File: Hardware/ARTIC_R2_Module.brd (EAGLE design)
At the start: 21.6 x 33 mm, 94 parts, among them J1 U.FL, K1 TLP3475R, Q2 5.8A/30V/35mΩ, U1 ADM4210-1, U2 1.8V/100mA, U3 ARTIC_R2, U4 RFPA0133, U5 AS179-92LF, U6 3.0V, X1 CRYSTAL-TCXO-26MHZ

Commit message: Work in progress
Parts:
- added J10, J11, J12, J13, J14, J15, J16, J17, J18, J19, J2, J20, J21, J22, J23, J24, J3, J4, J5, J6, J7, J8, J9: (no value), SparkFun-Connectors:1X01_NO_SILK
- added J25: U.FL, SparkFun-Connectors:U.FL
- added U$2: (no value), output:10
- J1: value U.FL -> (none); device SparkFun-Connectors:U.FL -> SparkFun-Connectors:1X01_NO_SILK
- moved J1 18.9 mm to (0.00, 30.5), turned to 0 degrees
- moved FD3 6.71 mm to (1.27, 1.27)
- moved FD4 6.71 mm to (1.27, 1.27)
- moved FD1 2.54 mm to (19.1, 31.8)
- moved FD2 2.54 mm to (19.1, 31.8)
- moved C3 1.97 mm to (6.35, 3.56)
- moved U2 1.97 mm to (4.25, 3.75)
- moved C45 1.89 mm to (8.38, 4.06)
- moved C2 1.80 mm to (10.0, 2.79)
- moved C23 1.69 mm to (11.8, 2.79)
- moved C49 1.69 mm to (9.53, 4.32)
- moved R11 1.69 mm to (10.5, 4.32)
- moved R12 1.69 mm to (12.8, 2.79)
- moved R2 1.69 mm to (12.3, 4.83)
- moved U1 1.69 mm to (16.1, 3.43)
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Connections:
- net ANTENNA: now also J23.1, J25.FEED; no longer J1.FEED
- net FLSH_CEN: now also J20.1
- net FLSH_SCLK: now also J17.1
- net FLSH_SI: now also J18.1
- net FLSH_SO: now also J19.1
- net GND: now also J16.1, J22.1, J24.1, J25.1, J25.2; no longer J1.1, J1.2
- net PWR_EN: now also J13.1
- net VDD: now also J21.1
- net VIN: now also J14.1, J15.1
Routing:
- net FLSH_CEN: track 0.00 -> 12.5 mm, vias 0 -> 1
- net FLSH_SO: track 0.00 -> 11.5 mm, vias 0 -> 1
- net FLSH_SI: track 0.00 -> 9.16 mm, vias 0 -> 1
- net FLSH_SCLK: track 0.00 -> 8.33 mm, vias 0 -> 1
- net VDD: track 74.1 -> 81.6 mm
- net PWR_EN: track 2.08 -> 8.60 mm
- net VIN: track 7.30 -> 12.2 mm
- net N$14: track 2.87 -> 6.70 mm
- net ANTENNA: track 1.54 -> 5.13 mm
- net 1.8V: track 64.0 -> 65.8 mm, vias 7 -> 8
- net N$2: track 4.50 -> 5.38 mm
- net N$3: track 7.92 -> 8.57 mm
- net GND: track 83.3 -> 83.4 mm, vias 103 -> 105
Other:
- board size 21.6 x 33 mm -> 20.3 x 33 mm
- board text added: "JLCPCB JLC7628 4-Layer 0.8mm Impedance Control 4-Layer Board 0.8mm Thickness 1oz Copper (Outer layers) ENIG Finish Castellated Holes When running the panelizer, add a horizontal gap of 0.5" to allow the castellated holes to be routed out"
- board text removed: "JLCPCB JLC7628 4-Layer 0.8mm Impedance Control 4-Layer Board 0.8mm Thickness 1oz Copper (Outer layers) ENIG Finish"

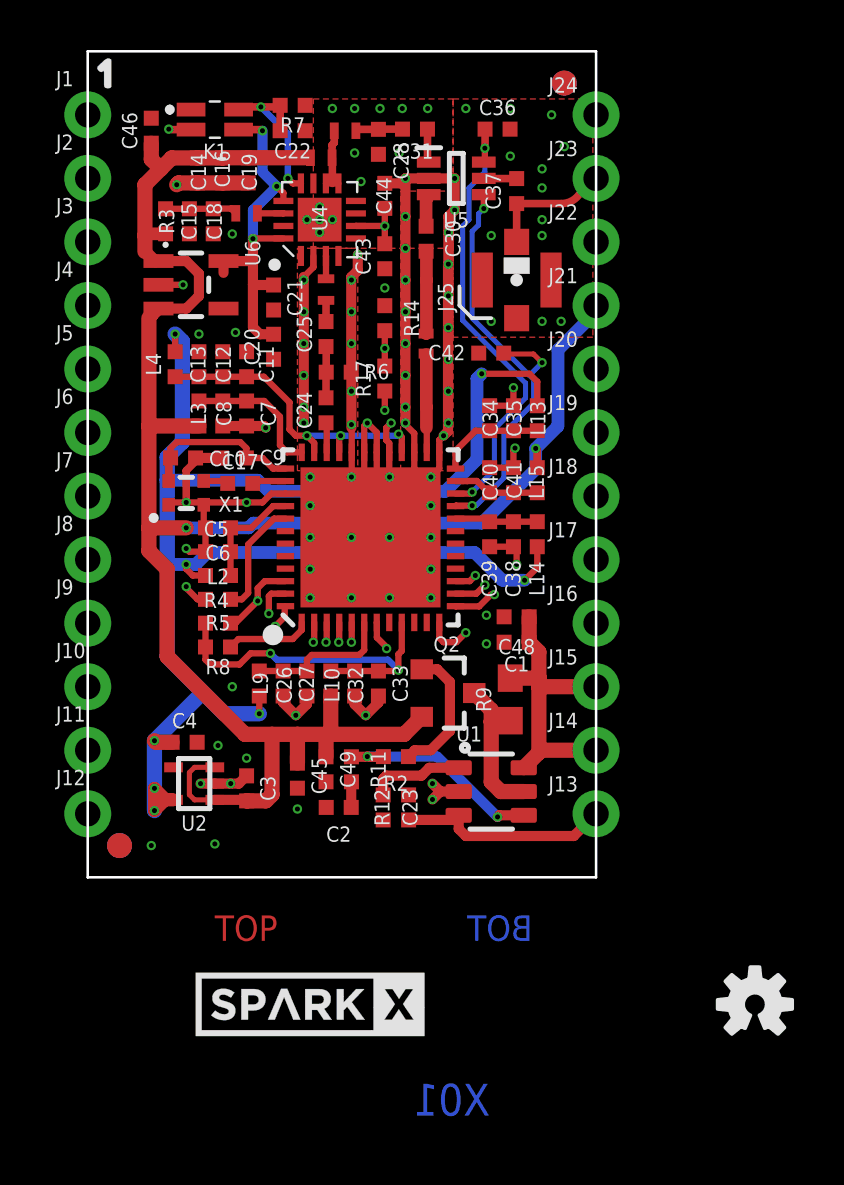
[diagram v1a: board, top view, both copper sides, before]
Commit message: Adding panel files. Updating README.
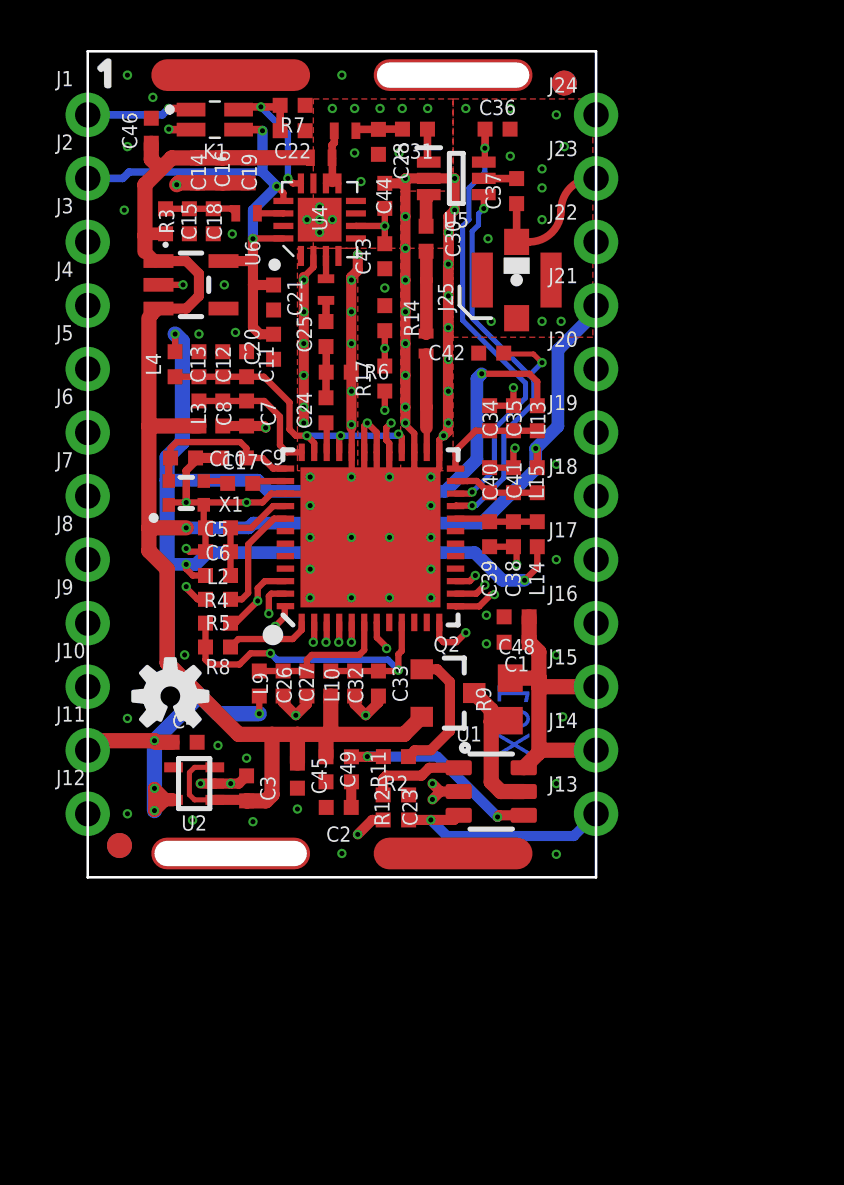
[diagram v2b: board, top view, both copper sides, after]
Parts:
- removed LOGO3: OSHW-LOGOS, SparkFun-Aesthetics:OSHW-LOGO-S
- removed SPARKX1, SPARKX2: SPARKX-LOGO4, SparkX:SPARKX-MEDIUM
- added SCREEN: ARTIC_R2_CASTELLATED_CAN, New_Parts_Screening_Cans:ARTIC_R2_CASTELLATED
- J1, J10, J11, J12, J13, J14, J15, J16, J17, J18, J19, J2, J20, J21, J22, J23, J24, J3, J4, J5, J6, J7, J8, J9: device SparkFun-Connectors:1X01_NO_SILK -> New_Parts_Connectors:1X01_CASTELLATED
- R9: value 0.012R -> 0.1R; device New_Parts:0603 -> New_Parts_Resistors:0603
- U1: device New_Parts:TSOT6 -> New_Parts_IC-Power:TSOT6
- moved LOGO2 26.4 mm to (3.30, 7.24)
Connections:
- net 1.8V: now also J11.1
- net BOOT: now also J3.1
- net CIPO: now also J10.1
- net COPI: now also J9.1
- net CS: now also J7.1
- net G8: now also J1.1
- net GND: now also J12.1, SCREEN.P$1, SCREEN.P$2, SCREEN.P$3, SCREEN.P$4
- net INT1: now also J4.1
- net INT2: now also J5.1
- net RESETB: now also J6.1
- net SCLK: now also J8.1
- net VREF1: now also J2.1
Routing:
- net BOOT: track 3.19 -> 22.2 mm
- net INT1: track 1.40 -> 19.0 mm
- net INT2: track 0.98 -> 16.9 mm
- net CS: track 0.81 -> 16.0 mm
- net RESETB: track 3.43 -> 17.4 mm
- net SCLK: track 0.80 -> 14.6 mm
- net COPI: track 0.80 -> 13.6 mm
- net CIPO: track 0.80 -> 13.6 mm
- net VREF1: track 15.6 -> 22.2 mm
- net PA_PD: track 16.4 -> 12.1 mm
- net G8: track 0.00 -> 4.25 mm, vias 0 -> 1
- net 1.8V: track 65.8 -> 68.6 mm
- net GND: track 83.4 -> 84.7 mm, vias 105 -> 120
- net PWR_EN: track 8.60 -> 9.32 mm, vias 0 -> 1
- net ANTENNA: track 5.13 -> 5.76 mm
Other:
- board text added: "Dimensions in Inches"
- board text added: "JLCPCB JLC7628 4-Layer 0.8mm Impedance Control 4-Layer Board 0.8mm Thickness 1oz Copper (Outer layers) ENIG Finish Castellated Holes When running the panelizer, add a vertical gap of 0.2" to allow the castellated holes to be routed out"
- board text removed: "15"
- board text removed: "2"
- board text removed: "BOT"
- board text removed: "JLCPCB JLC7628 4-Layer 0.8mm Impedance Control 4-Layer Board 0.8mm Thickness 1oz Copper (Outer layers) ENIG Finish Castellated Holes When running the panelizer, add a horizontal gap of 0.5" to allow the castellated holes to be routed out"
- board text removed: "TOP"

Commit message: Adding better castellated pads. Correcting cutouts for screen tabs.
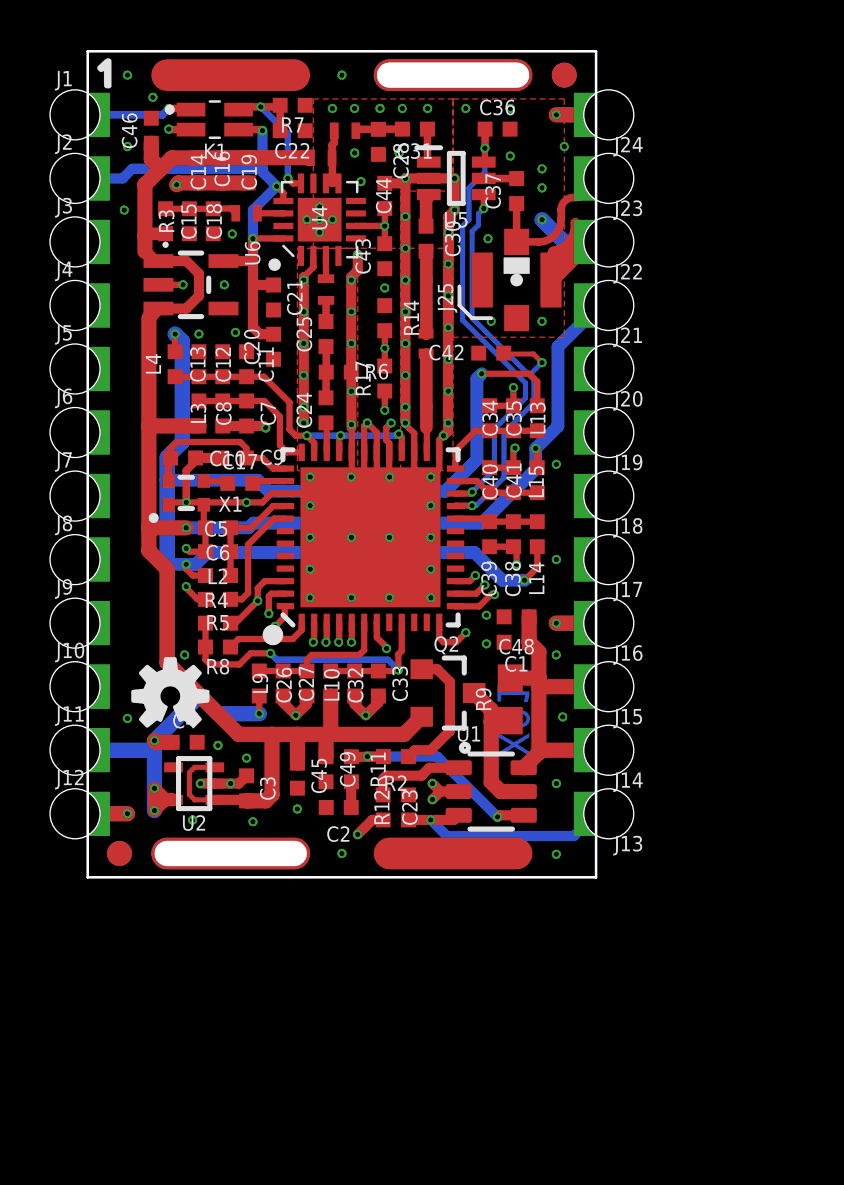
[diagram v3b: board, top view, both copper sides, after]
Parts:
- added LOGO3: OSHW-LOGOS, SparkFun-Aesthetics:OSHW-LOGO-S
- added SPARKX2: SPARKX-LOGO4, SparkX:SPARKX-MEDIUM
- added U$1, U$3, U$4, U$5: (no value), output:#GND#0
- added U$10: (no value), output:#FLSH_SI#0
- added U$11: (no value), output:#FLSH_SO#0
- added U$12: (no value), output:#FLSH_CEN#0
- added U$13: (no value), output:#3#3V_OUT#0
- added U$14: (no value), output:#ANTENNA#0
- added U$15: (no value), output:#G8#0
- added U$16: (no value), output:#3#0V_OUT#0
- added U$17: (no value), output:#BOOT#0
- added U$18: (no value), output:#INT1#0
- added U$19: (no value), output:#INT2#0
- added U$20: (no value), output:#RESETB#0
- added U$21: (no value), output:#CS#0
- added U$22: (no value), output:#SCLK#0
- added U$23: (no value), output:#COPI#0
- added U$24: (no value), output:#CIPO#0
- added U$25: (no value), output:#1#8V_OUT#0
- added U$26: (no value), output:ARTIC_R20
- added U$6: (no value), output:#PWR_EN#0
- added U$7, U$8: (no value), output:#VIN#0
- added U$9: (no value), output:#FLSH_SCLK#0
- J1, J10, J11, J12, J13, J14, J15, J16, J17, J18, J19, J2, J20, J21, J22, J23, J24, J3, J4, J5, J6, J7, J8, J9: device New_Parts_Connectors:1X01_CASTELLATED -> New_Parts_Connectors:CONN_01_CASTELLATED_4LAYER
- moved FD1 0.32 mm to (19.1, 32.1)
- moved FD2 0.32 mm to (19.1, 32.1)
- moved FD3 0.32 mm to (1.27, 0.95)
- moved FD4 0.32 mm to (1.27, 0.95)
- turned J13 to 180 degrees
- turned J14 to 180 degrees
- turned J15 to 180 degrees
- turned J16 to 180 degrees
- turned J17 to 180 degrees
- turned J18 to 180 degrees
- turned J19 to 180 degrees
- turned J20 to 180 degrees
- turned J21 to 180 degrees
- turned J22 to 180 degrees
- turned J23 to 180 degrees
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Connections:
- net GND: now also SCREEN.1-1, SCREEN.1-16, SCREEN.2, SCREEN.3-1, SCREEN.3-16, SCREEN.4; no longer SCREEN.P$1, SCREEN.P$2, SCREEN.P$3, SCREEN.P$4
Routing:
- net GND: track 84.7 -> 117.5 mm

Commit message: Updated the screening can
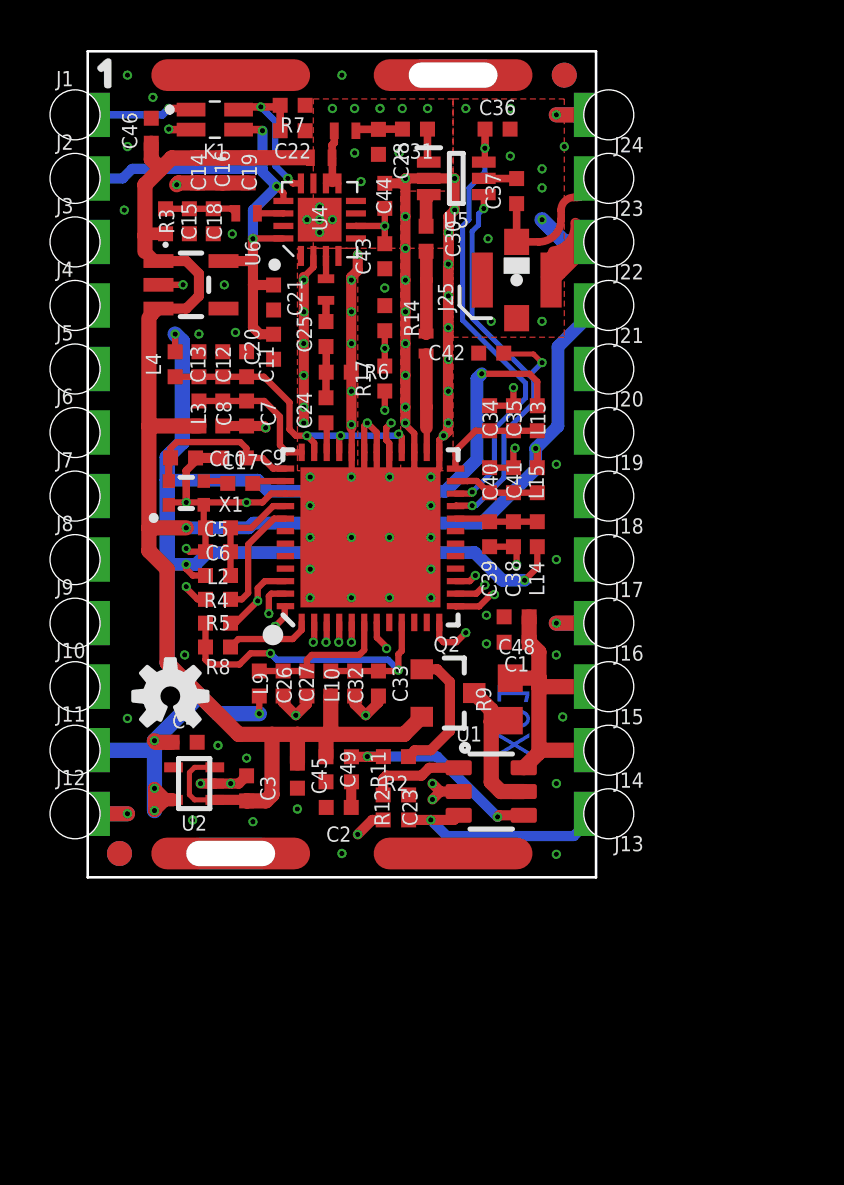
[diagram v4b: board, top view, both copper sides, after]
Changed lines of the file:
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@@
 <via x="6.9215" y="30.7975" extent="1-16" drill="0.2"/>
 <contactref element="K1" pad="4"/>
-<wire x1="8.001" y1="27.94" x2="8.001" y2="29.718" width="0.254" layer="16"/>
-<wire x1="8.001" y1="29.718" x2="6.9215" y2="30.7975" width="0.254" layer="16"/>
+<wire x1="7.493" y1="30.226" x2="7.493" y2="28.448" width="0.254" layer="16"/>
+<wire x1="8.001" y1="27.94" x2="7.493" y2="28.448" width="0.254" layer="16"/>
+<wire x1="7.493" y1="30.226" x2="6.9215" y2="30.7975" width="0.254" layer="16"/>
 <wire x1="6.03" y1="30.6895" x2="6.138" y2="30.7975" width="0.3048" layer="1"/>
 <wire x1="6.138" y1="30.7975" x2="6.9215" y2="30.7975" width="0.3048" layer="1"/>
